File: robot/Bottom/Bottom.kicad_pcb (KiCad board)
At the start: 2 copper layers, 46 x 46 mm, 37 parts, among them M1 Stepper_Motor_bipolar, M2 Stepper_Motor_bipolar, U1 GP2S60, U2 GP2S60, U7 DRV8833PWP, U8 DRV8833PWP

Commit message: Start renumber
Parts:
- moved R13 55.5 mm to (177.0, 117.5), turned to 270 degrees
- moved R14 54.5 mm to (180.1, 117.5), turned to 270 degrees
- moved C12 40.7 mm to (175.5, 104.2), turned to 90 degrees
- moved C13 30.2 mm to (178.5, 104.2), turned to 90 degrees
- moved R3 29.3 mm to (190.7, 87.6), turned to 90 degrees
- moved U2 27.0 mm to (192.1, 81.3)
- moved C11 25.5 mm to (181.5, 104.2), turned to 270 degrees
- moved U8 24.7 mm to (178.6, 111.2), turned to 90 degrees
- moved R4 21.1 mm to (193.8, 87.6), turned to 90 degrees
- moved M2 9.65 mm to (187.8, 111.2), turned to 270 degrees

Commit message: Renumber and more Bottom
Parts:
- moved H10 17.8 mm to (180.6, 77.0)
- moved H4 17.8 mm to (162.8, 77.0)
- moved H3 12.7 mm to (165.4, 77.0)
- moved H9 12.7 mm to (178.1, 77.0)
- moved H2 7.62 mm to (167.9, 77.0)
- moved H8 7.62 mm to (175.5, 77.0)
- moved H1 2.54 mm to (170.4, 77.0)
- moved H7 2.54 mm to (173.0, 77.0)
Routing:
- net +3V3: track 0.00 -> 20.3 mm
- net Net-(H5-Pad1): track 0.00 -> 18.4 mm, vias 0 -> 2
- net Net-(H6-Pad1): track 0.00 -> 11.2 mm
- net Net-(C9-Pad1): track 0.00 -> 3.74 mm
- net Net-(C8-Pad2): track 0.00 -> 3.74 mm
- net Net-(C12-Pad1): track 0.00 -> 3.71 mm
- net Net-(C11-Pad2): track 0.00 -> 3.70 mm
- net Net-(R2-Pad2): track 0.00 -> 2.29 mm
- net Net-(R13-Pad1): track 0.00 -> 2.28 mm
- net Net-(R14-Pad1): track 0.00 -> 2.24 mm
- net Net-(R12-Pad1): track 0.00 -> 2.24 mm
- net Net-(R11-Pad1): track 0.00 -> 2.24 mm
- net Net-(R4-Pad2): track 0.00 -> 2.14 mm
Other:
- net class Power added: clearance 0.3, trace_width 0.5, via_dia 1, via_drill 0.5

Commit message: Finish bottom
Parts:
- added H18: GND_TOUCH, Custom:Mounting_Pad_Ground, B.Cu at (153.2, 78.2)
- added H19: GND_TOUCH, Custom:Mounting_Pad_Ground, B.Cu at (192.8, 78.2)
- H16, H17: footprint Custom:Mounting_Pad_Power -> Custom:Mounting_Pad_Ground; moved to B.Cu
- moved H17 42.6 mm to (179.6, 78.2)
- moved H16 33.9 mm to (166.4, 78.2)
- moved C11 0.84 mm to (182.3, 104.0)
- moved C12 0.84 mm to (174.7, 104.0)
- moved C8 0.84 mm to (171.3, 104.0)
- moved C9 0.84 mm to (163.7, 104.0)
- moved U7 0.35 mm to (167.5, 110.9)
- moved U8 0.35 mm to (178.6, 110.9)
- moved R11 0.30 mm to (165.7, 117.5)
- moved C10 0.25 mm to (167.5, 104.0), turned to 180 degrees
- moved C13 0.25 mm to (178.5, 104.0), turned to 180 degrees
- moved R14 0.20 mm to (180.3, 117.5)
- moved R12 0.20 mm to (169.2, 117.5)
- moved R13 0.20 mm to (176.8, 117.5)
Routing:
- net +3V3: track 20.3 -> 100.7 mm, vias 0 -> 6
- net /M1_~SLEEP: track 0.00 -> 59.8 mm, vias 0 -> 3
- net /M1_AIN1: track 0.00 -> 38.2 mm
- net /M2_BIN1: track 0.00 -> 36.9 mm, vias 0 -> 2
- net /M1_AIN2: track 0.00 -> 36.5 mm, vias 0 -> 2
- net /M2_BIN2: track 0.00 -> 35.0 mm
- net /M1_BIN2: track 0.00 -> 33.9 mm, vias 0 -> 2
- net /M1_BIN1: track 0.00 -> 33.4 mm, vias 0 -> 2
- net /M2_AIN1: track 0.00 -> 32.6 mm, vias 0 -> 2
- net /M2_AIN2: track 0.00 -> 31.8 mm, vias 0 -> 2
- net GND: track 0.00 -> 22.4 mm, vias 0 -> 18
- net Net-(M2-Pad1): track 0.00 -> 21.4 mm
- net Net-(M1-Pad3): track 0.00 -> 17.7 mm
- net Net-(M1-Pad4): track 0.00 -> 13.6 mm, vias 0 -> 1
- net Net-(M1-Pad2): track 0.00 -> 13.3 mm, vias 0 -> 1
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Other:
- outline, holes or cut-outs redrawn

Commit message: Bottem changes
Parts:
- M1, M2: footprint Custom:K976_Stepper -> Custom:Medium_Stepper
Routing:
- net Net-(M2-Pad1): track 21.4 -> 20.6 mm
- net Net-(M1-Pad3): track 17.7 -> 18.3 mm
- net Net-(M2-Pad3): track 10.9 -> 10.4 mm
- net Net-(M1-Pad2): track 13.3 -> 12.8 mm
- net GND: vias 18 -> 17

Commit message: Finisch bottom
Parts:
- C10, C11, C12, C13, C8, C9: footprint Capacitors_SMD:C_1206 -> Capacitors_SMD:C_0805
- R1, R11, R12, R13, R14, R2, R3, R4: footprint Resistors_SMD:R_1206 -> Resistors_SMD:R_0805
- moved C11 4.73 mm to (178.2, 101.5)
- moved C9 4.73 mm to (167.8, 101.5)
- moved H12 3.87 mm to (188.3, 80.5)
- moved H13 3.87 mm to (154.2, 80.5)
- moved H14 3.87 mm to (191.8, 80.5)
- moved H15 3.87 mm to (157.7, 80.5)
- moved U2 3.36 mm to (189.8, 83.8)
- moved M1 3.35 mm to (161.2, 112.8)
- moved M2 3.35 mm to (184.8, 112.8)
- moved U1 3.33 mm to (155.8, 83.8)
- moved H6 3.27 mm to (185.7, 80.0)
- moved H5 3.27 mm to (160.3, 80.0)
- moved H18 3.11 mm to (155.4, 80.5)
- moved H19 3.11 mm to (190.6, 80.5)
- moved H1 3.00 mm to (170.4, 80.0)
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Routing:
- net /M1_~SLEEP: track 60.0 -> 50.4 mm
- net /M1_AIN1: track 38.2 -> 29.7 mm, vias 0 -> 2
- net /M1_AIN2: track 36.5 -> 28.5 mm, vias 2 -> 0
- net Net-(M2-Pad1): track 20.6 -> 12.7 mm, vias 0 -> 1
- net /M2_BIN2: track 35.0 -> 28.5 mm
- net /M2_BIN1: track 36.9 -> 30.5 mm
- net Net-(M1-Pad3): track 18.3 -> 13.5 mm, vias 0 -> 1
- net /M2_AIN1: track 32.6 -> 27.9 mm
- net +3V3: track 100.7 -> 104.7 mm, vias 6 -> 8
- net GND: track 22.4 -> 25.7 mm, vias 17 -> 25
- net /M2_AIN2: track 31.8 -> 28.9 mm, vias 2 -> 0
- net /M1_BIN1: track 33.4 -> 30.8 mm
- net Net-(H5-Pad1): track 18.4 -> 16.4 mm, vias 2 -> 0
- net Net-(M2-Pad3): track 10.4 -> 8.47 mm
- net Net-(H6-Pad1): track 11.7 -> 9.98 mm
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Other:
- board size 46 x 46 mm -> 40 x 40 mm
- net class Default: trace_width 0.25 -> 0.2
- net class Power: trace_width 0.5 -> 0.4

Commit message: Changes to bottom, 3D export
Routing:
- net Net-(M1-Pad1): vias 0 -> 1
- net GND: vias 25 -> 24

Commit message: Small fixes, step files
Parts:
- moved C10 11.9 mm to (166.0, 93.3)
- moved C11 11.9 mm to (182.0, 90.3)
- moved C12 11.9 mm to (178.1, 90.3)
- moved C13 11.9 mm to (180.1, 93.3)
- moved C8 11.9 mm to (167.9, 90.3)
- moved C9 11.9 mm to (164.0, 90.3)
- moved R11 11.9 mm to (164.0, 105.0)
- moved R12 11.9 mm to (167.9, 105.0)
- moved R13 11.9 mm to (178.1, 105.0)
- moved R14 11.9 mm to (182.0, 105.0)
- moved U7 11.9 mm to (166.0, 98.9)
- moved U8 11.9 mm to (180.1, 98.9)
- moved M1 2.50 mm to (163.8, 112.8)
- moved M2 2.50 mm to (182.2, 112.8)
- moved H16 0.75 mm to (167.2, 80.5)
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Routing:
- net +3V3: track 104.7 -> 78.5 mm
- net Net-(M2-Pad1): track 12.7 -> 27.4 mm, vias 1 -> 0
- net /M1_BIN2: track 33.9 -> 20.9 mm, vias 2 -> 0
- net /M2_BIN1: track 30.5 -> 19.2 mm
- net /M2_AIN2: track 28.9 -> 18.0 mm
- net /M2_BIN2: track 28.5 -> 18.5 mm
- net /M2_AIN1: track 27.9 -> 18.5 mm, vias 2 -> 0
- net /M1_BIN1: track 30.8 -> 21.6 mm, vias 2 -> 0
- net /M1_AIN2: track 28.5 -> 20.7 mm, vias 0 -> 2
- net (no net): track 0.00 -> 7.60 mm, vias 0 -> 4
- net /M1_AIN1: track 29.7 -> 24.1 mm
- net Net-(M1-Pad1): track 8.48 -> 13.8 mm, vias 1 -> 0
- net Net-(M1-Pad3): track 13.5 -> 18.2 mm, vias 1 -> 0
- net Net-(M2-Pad3): track 8.47 -> 11.9 mm
- net /M1_~SLEEP: track 50.4 -> 47.4 mm, vias 3 -> 4
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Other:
- outline, holes or cut-outs redrawn

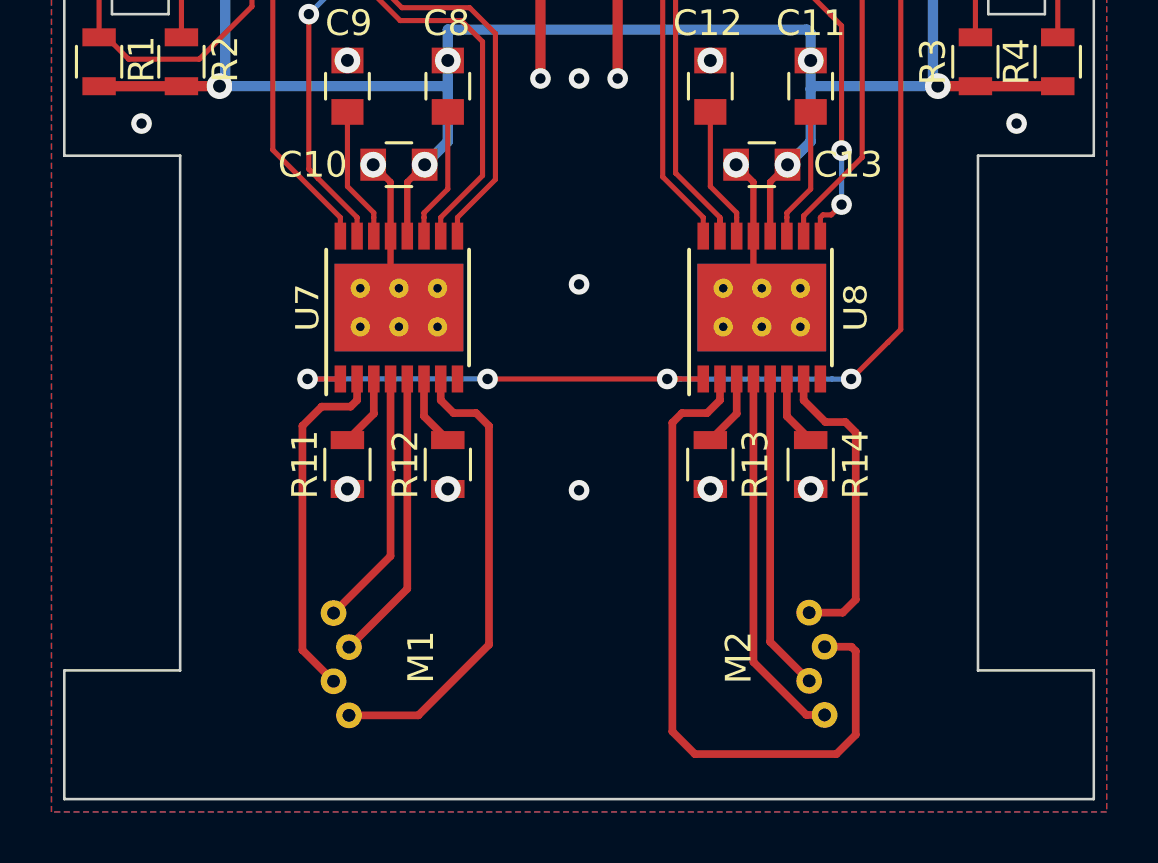
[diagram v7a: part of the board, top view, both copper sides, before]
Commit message: Move Motors
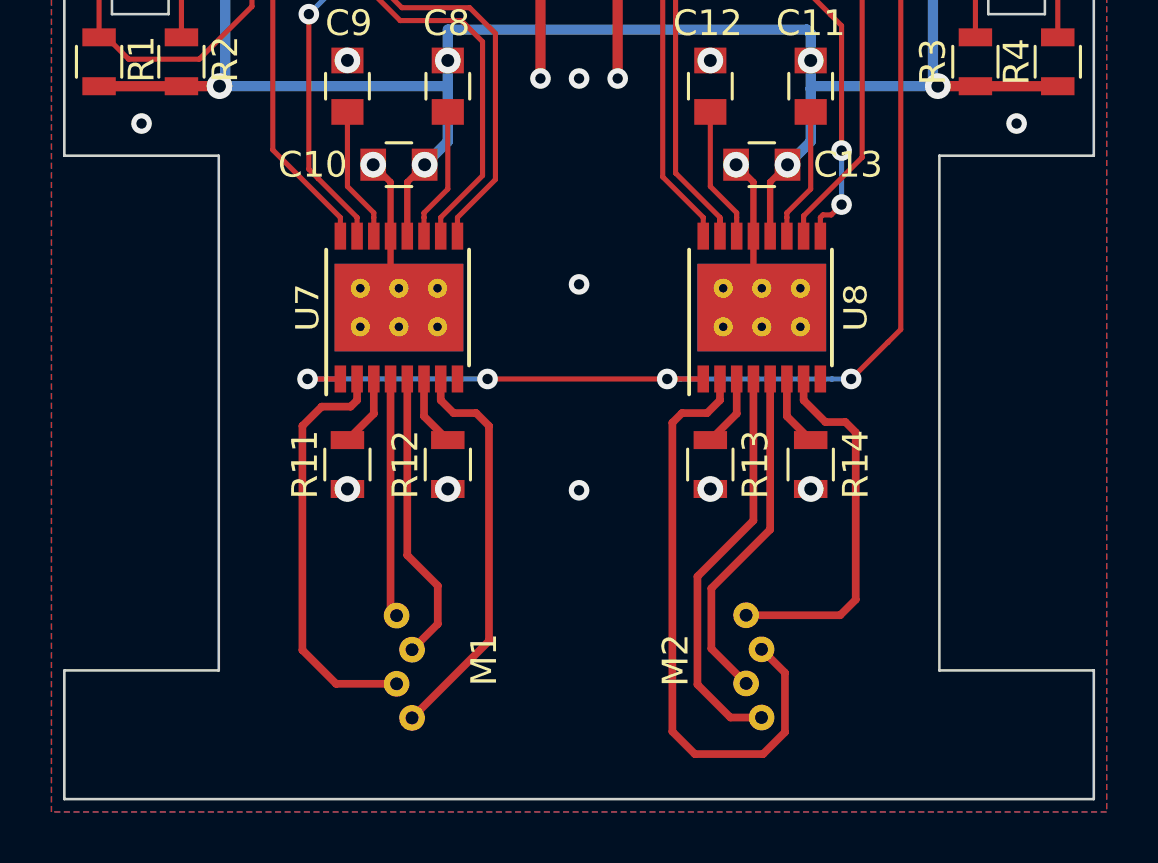
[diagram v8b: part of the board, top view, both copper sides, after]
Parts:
- moved M1 2.45 mm to (166.2, 112.8)
- moved M2 2.45 mm to (179.8, 112.8)
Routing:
- net Net-(M2-Pad1): track 27.4 -> 23.7 mm
- net Net-(M1-Pad3): track 18.2 -> 15.7 mm
- net Net-(M2-Pad3): track 11.9 -> 14.4 mm
- net Net-(M1-Pad1): track 13.8 -> 16.3 mm
- net Net-(M2-Pad2): track 14.6 -> 15.8 mm
- net Net-(M2-Pad4): track 12.4 -> 13.3 mm
- net Net-(M1-Pad2): track 10.0 -> 9.29 mm
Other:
- outline, holes or cut-outs redrawn
